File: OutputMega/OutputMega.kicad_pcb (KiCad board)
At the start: 2 copper layers, 78.7 x 92.1 mm, 134 parts, among them J1 Control, J10 Conn_02x13_Top_Bottom, J11 EStop Sig1 JST2H, J12 MegaProMiniR, J13 JTAG, J14 Dbg, J15 EStop Rly JST2H, J16 Sp Rly 1 JST2H, J17 Sp Rly 2 JST2H, J18 Step Disable JST2H, J19 EStop Sig0 JST2H, J2 EStop JST3H, J20 EStop Sig1 JST2H, J21 Conn_01x06_Male, J22 Conn_02x05_Odd_Even, J23 Sw 12v 1 JST2H, J24 Sw 12v 2 JST2H, J25 Pilot JST2H, J26 VFD Dir JST3H, J27 VFD Ctl JST3H, J3 EStop Rst JST2H, J4 TmrTest, J5 DbgPort, J6 RemPort, J7 12VIn, J8 PwrIn, J9 MegaProMiniL, K1 G6S-2, K2 G6S-2, K3 G6S-2, Q1 2N7002, Q10 2N7002, Q11 2N7002, Q12 2N7002, Q13 2N7002, Q2 2N7002, Q3 2N7002, Q4 2N7002, Q5 2N7002, Q6 2N7002, Q7 2N7002, Q8 2N7002, Q9 2N7002, U1 74HCT123, U10 MC34072AP, U2 74LS08, U3 LD1117S50TR_SOT223, U4 74LVC2G00, U5 74AUC2G34, U6 74AUC2G34, U7 74LVC2G157, U8 74LS08, U9 TLV9351

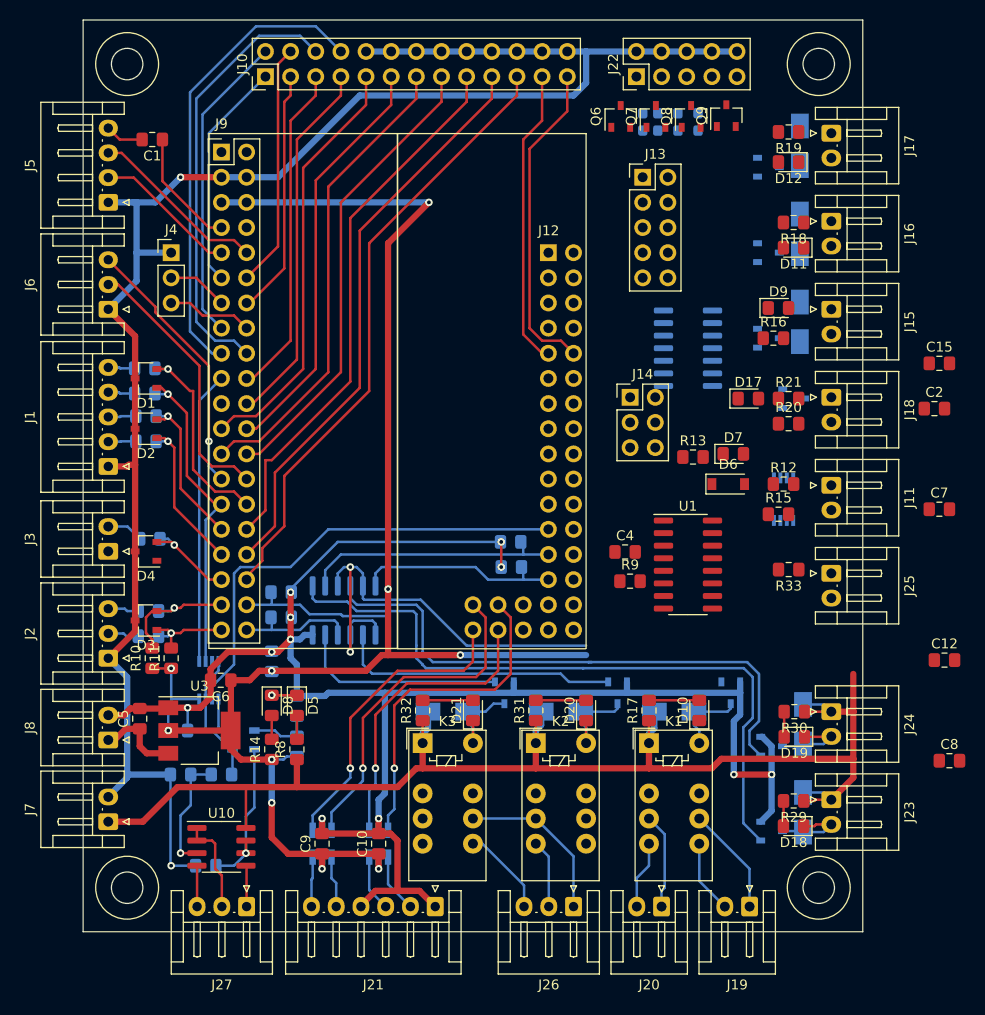
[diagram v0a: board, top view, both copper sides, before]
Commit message: Output Mega layout completed.
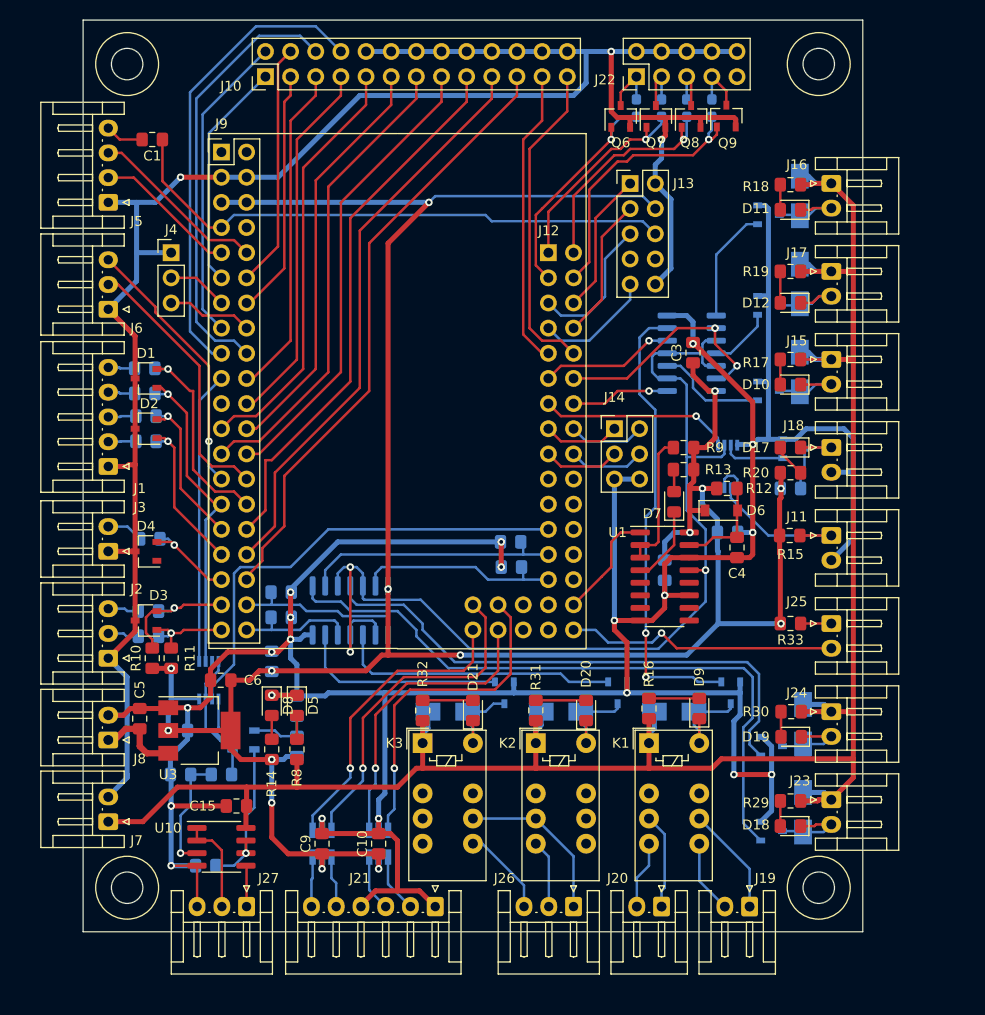
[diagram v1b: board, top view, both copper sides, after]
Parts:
- removed C8: .1uf, Capacitor_SMD:C_0805_2012Metric_Pad1.15x1.40mm_HandSolder
- C12, C2, C7, R21: moved to B.Cu
- C3: moved to F.Cu
- J1: footprint Connector_JST:JST_EH_S5B-EH_1x05_P2.50mm_Horizontal -> 0MiscParts:JST_EH_S5B-EH_1x05_P2.50mm_Horizontal
- J11, J15, J16, J17, J18, J19, J20, J23, J24, J25, J3, J7, J8: footprint Connector_JST:JST_EH_S2B-EH_1x02_P2.50mm_Horizontal -> 0MiscParts:JST_EH_S2B-EH_1x02_P2.50mm_Horizontal
- J2, J26, J27, J6: footprint Connector_JST:JST_EH_S3B-EH_1x03_P2.50mm_Horizontal -> 0MiscParts:JST_EH_S3B-EH_1x03_P2.50mm_Horizontal
- J5: footprint Connector_JST:JST_EH_S4B-EH_1x04_P2.50mm_Horizontal -> 0MiscParts:JST_EH_S4B-EH_1x04_P2.50mm_Horizontal
- moved C15 83.9 mm to (103.8, 142.2), turned to 180 degrees
- moved C12 67.9 mm to (107.3, 127.6), turned to 90 degrees
- moved C3 52.7 mm to (149.9, 96.5)
- moved D9 41.2 mm to (150.5, 132.4), turned to 90 degrees
- moved R16 39.5 mm to (145.4, 132.4), turned to 90 degrees
- moved R17 38.2 mm to (159.7, 97.1), turned to 180 degrees
- moved D10 34.2 mm to (159.7, 99.7), turned to 180 degrees
- moved C2 31.8 mm to (147.0, 118.4), turned to 270 degrees
- moved C7 21.5 mm to (153.4, 114.6)
- moved R9 14.5 mm to (148.9, 106.0), turned to 180 degrees
- moved D12 14.2 mm to (159.7, 91.4)
- moved R19 14.1 mm to (159.7, 88.3)
- moved D16 14.0 mm to (160.7, 89.5)
- moved J17 14.0 mm to (163.8, 88.3)
- moved Q4 14.0 mm to (157.5, 91.7)
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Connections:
- net /EGR renamed /ESSR
- net /ESR renamed /ESRR
- net /EStopRlyDrv renamed /EStopRlyExt
- D17 pad 1: /DsR -> /StepDisDrv
- D17 pad 2: +5V -> /DsR
- R20 pad 1: /DsR -> +5V
- R20 pad 2: /StepDisDrv -> /DsR
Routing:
- net GND: track 380.0 -> 566.1 mm, vias 14 -> 23
- net +5V: track 161.7 -> 266.9 mm, vias 10 -> 15
- net +12V: track 137.2 -> 218.7 mm
- net /WDOut: track 46.7 -> 105.9 mm, vias 2 -> 3
- net /EStopSigOut: track 0.00 -> 46.4 mm, vias 0 -> 2
- net /Reset: track 12.1 -> 57.2 mm
- net /Ctl4Out: track 0.00 -> 27.9 mm, vias 0 -> 1
- net /Pilot: track 0.00 -> 27.6 mm, vias 0 -> 1
- net /ProcSpindleRly: track 0.00 -> 23.7 mm, vias 0 -> 2
- net /Ctl1Out: track 0.00 -> 23.1 mm, vias 0 -> 1
- net /Ctl3Out: track 0.00 -> 22.9 mm, vias 0 -> 1
- net /Ctl2Out: track 0.00 -> 21.2 mm, vias 0 -> 1
- net /ProcStepDis: track 0.00 -> 19.3 mm, vias 0 -> 1
- net /ExtStepDis: track 0.00 -> 15.9 mm
- net /TDO: track 0.00 -> 14.4 mm
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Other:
- net class Power added: clearance 0.2032, trace_width 0.508, via_dia 0.762, via_drill 0.381

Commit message: Add labels to silk screen.
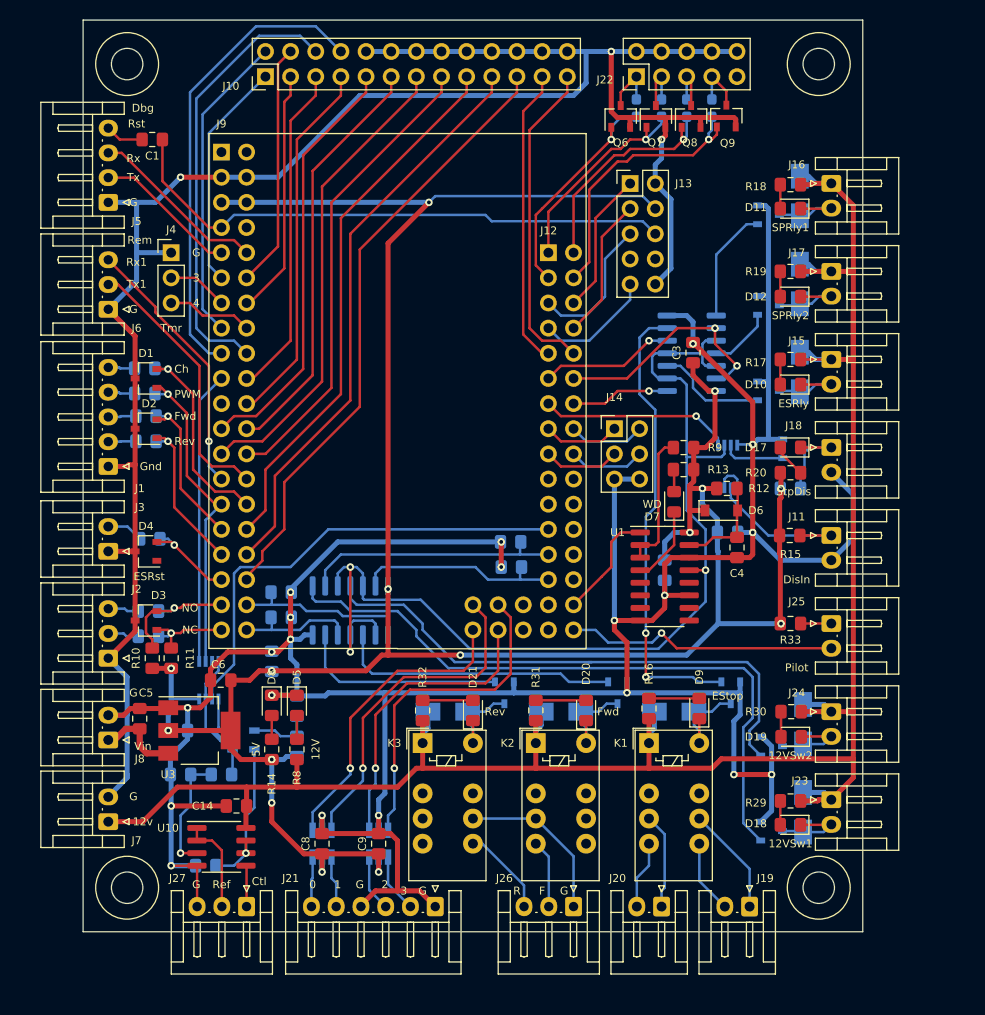
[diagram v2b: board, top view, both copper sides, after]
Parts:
- moved D12 0.62 mm to (159.7, 90.8)
- moved D18 0.13 mm to (159.7, 144.1)
- moved D11 0.11 mm to (159.7, 81.9)
- renumbered C11 to C10, C12 to C11, C13 to C12, C14 to C13, C15 to C14, C9 to C8, C10 to C9
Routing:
- net GND: track 566.1 -> 563.4 mm
- net /Sp2R: track 3.17 -> 2.55 mm
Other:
- board text added: "0"
- board text added: "1"
- board text added: "12V"
- board text added: "12VSw1"
- board text added: "12VSw2"
- board text added: "12v"
- board text added: "2"
- board text added: "3"
- board text added: "4"
- board text added: "5V"
- board text added: "Ch"
- board text added: "Ctl"
- board text added: "Dbg"
- board text added: "DisIn"
- board text added: "ESRly"
- board text added: "ESRst"
- board text added: "EStop"
- board text added: "F"
- board text added: "Fwd"
- board text added: "G"
- board text added: "Gnd"
- board text added: "NC"
- board text added: "NO"
- board text added: "PWM"
- board text added: "Pilot"
- board text added: "R"
- board text added: "Ref"
- board text added: "Rem"
- board text added: "Rev"
- board text added: "Rst"
- board text added: "Rx"
- board text added: "Rx1"
- board text added: "SPRly1"
- board text added: "SPRly2"
- board text added: "StpDis"
- board text added: "Tmr"
- board text added: "Tx"
- board text added: "Tx1"
- board text added: "Vin"
- board text added: "WD"

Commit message: Designed front panel.  More updates to output.
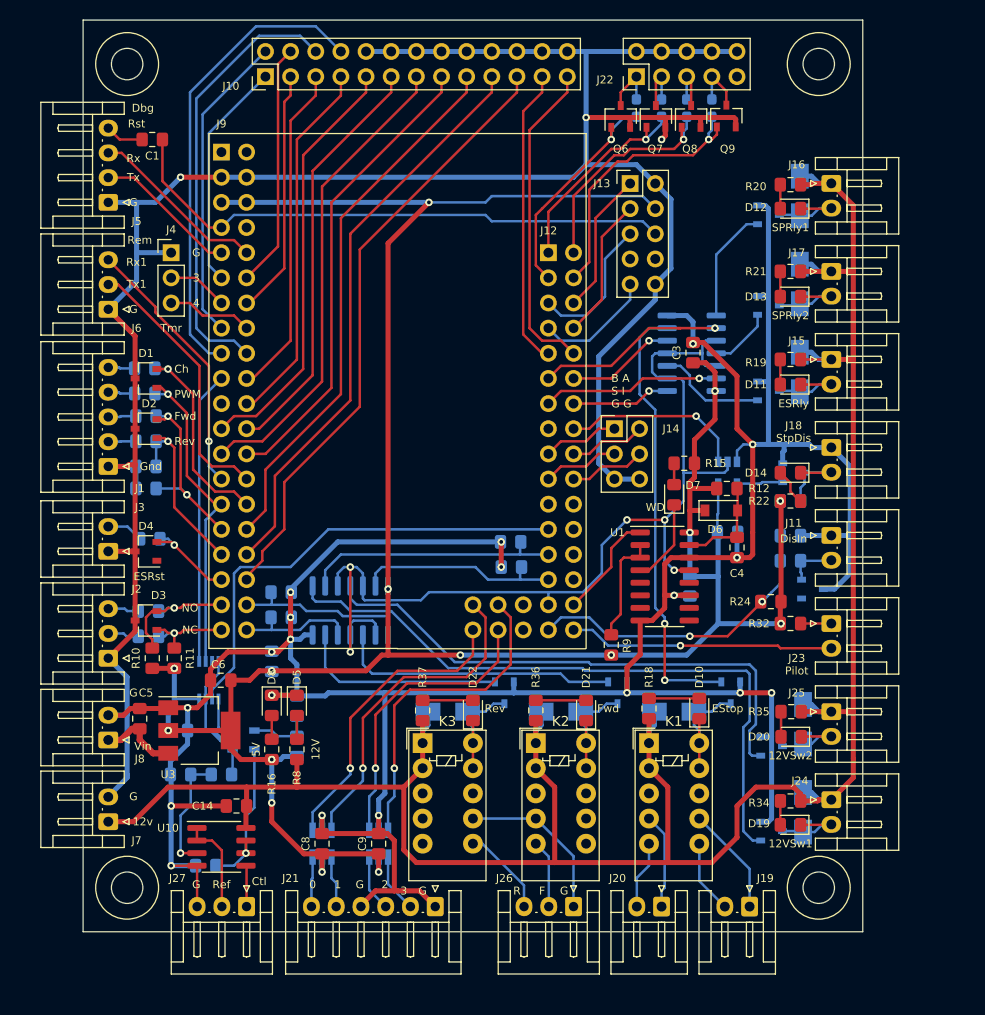
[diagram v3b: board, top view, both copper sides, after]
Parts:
- added D9: D_Zener_x2_ACom_KKA, 0MiscParts:SOT-23-Handsoldering, B.Cu at (161.9, 120.3)
- added R13: 10k, Resistor_SMD:R_0805_2012Metric_Pad1.15x1.40mm_HandSolder, B.Cu at (94.6, 110.2)
- added R14: 10k, Resistor_SMD:R_0805_2012Metric_Pad1.15x1.40mm_HandSolder, B.Cu at (94.6, 108.0)
- added R17: 200, Resistor_SMD:R_0805_2012Metric_Pad1.15x1.40mm_HandSolder, B.Cu at (159.7, 117.5)
- added R25: 10k, Resistor_SMD:R_0805_2012Metric_Pad1.15x1.40mm_HandSolder, B.Cu at (159.7, 114.9)
- J1: value Control -> Control JST5H
- J11: value EStop Sig1 JST2H -> Ext Step Disable JST2H
- J13: value JTAG -> JTAG 2x05
- J14: value Dbg -> Dbg 2x03
- J4: value TmrTest -> TmrTest 1x03
- J5: value DbgPort -> DbgPort JST4H
- J6: value RemPort -> RemPort JST3H
- J7: value 12VIn -> 12VIn JST2H
- J8: value PwrIn -> PwrIn JST2H
- K1, K2, K3: footprint Relay_THT:Relay_DPDT_Omron_G6S-2 -> 0MiscParts:Relay_DPDT_Omron_G6S-2
- R24: renamed from R15; value R -> 10k
- U4: value 74LVC2G00 -> 74LVC1G08; footprint Package_SO:TSSOP-8_3x3mm_P0.65mm -> Package_TO_SOT_SMD:SOT-23-5
- moved R9 21.2 mm to (141.6, 126.0), turned to 90 degrees
- moved R24 6.95 mm to (157.7, 121.6), turned to 180 degrees
- moved C2 3.00 mm to (149.5, 120.0)
- moved R22 2.86 mm to (159.7, 111.4)
- moved D14 2.55 mm to (159.7, 108.6)
- moved Q5 2.43 mm to (160.0, 108.6)
- moved R23 1.27 mm to (159.7, 111.4)
- moved D7 0.71 mm to (148.0, 110.8)
- moved R15 0.64 mm to (149.0, 107.6)
- moved U4 0.63 mm to (153.4, 108.6)
- moved R11 0.32 mm to (97.5, 127.3)
- renumbered D9 to D10, D10 to D11, D11 to D12, D12 to D13, D17 to D14, D13 to D15, D14 to D16, D15 to D17, D16 to D18, D18 to D19, D19 to D20, D20 to D21, D21 to D22, D22 to D23, D23 to D24, D24 to D25, D25 to D26, J25 to J23, J23 to J24, J24 to J25, R13 to R15, R14 to R16, R16 to R18, R17 to R19, R18 to R20, R19 to R21, R20 to R22, R21 to R23, R22 to R26, R23 to R27, R24 to R28, R25 to R29, R26 to R30, R27 to R31, R33 to R32, R28 to R33, R29 to R34, R30 to R35, R31 to R36, R32 to R37
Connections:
- J11 pad 1: /ExtStepDis -> GND
- J11 pad 2: GND -> /StepDisIn
- J12 pad 51: /ProcEStopSig -> /ProcSpdlRly1
- J12 pad 52: /ProcSpindleRly -> /ProcEStopSig
- J12 pad 53: /ProcStepDis -> /ProcSpdlRly2
- J12 pad 55: /B -> (no net)
- J12 pad 56: /A -> /ProcStepDis
- J12 pad 57: /Sync -> /B
- J12 pad 58: /Index -> /A
- J12 pad 59: (no net) -> /Sync
- J12 pad 60: (no net) -> /Index
- J12 pad 69: (no net) -> /WDOut
- J12 pad 71: (no net) -> /ExtStepDis
- J18 pad 1: /StepDisDrv -> GND
- J18 pad 2: GND -> /StepDisDrv
- U2 pad 13: /ProcSpindleRly -> /ProcSpdlRly2
- U2 pad 9: /ProcSpindleRly -> /ProcSpdlRly1
- U4 pad 3: /StepDis -> GND
- U4 pad 4: GND -> /StepDis
- U4 pad 5: /StepDisOut -> +5V
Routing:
- net +12V: track 218.7 -> 248.4 mm
- net /ProcSpindleRly: track 23.7 -> 0.00 mm, vias 2 -> 0
- net GND: track 563.4 -> 586.6 mm, vias 23 -> 22
- net /ProcSpdlRly1: track 0.00 -> 19.2 mm, vias 0 -> 1
- net /ProcSpdlRly2: track 0.00 -> 18.0 mm, vias 0 -> 1
- net /ExtStepDis: track 15.9 -> 31.8 mm, vias 0 -> 2
- net /StepDisIn: track 0.00 -> 5.07 mm
- net /WDOut: track 105.9 -> 101.5 mm, vias 3 -> 5
- net /SpFwd: track 16.1 -> 19.5 mm, vias 1 -> 2
- net /StepDisOut: track 3.31 -> 0.00 mm
- net +5V: track 267.3 -> 264.4 mm
- net /WDPU: track 13.9 -> 11.2 mm
- net /RevDrv: track 9.72 -> 12.3 mm
- net /FwdDrv: track 9.72 -> 12.3 mm
- net /EStopRly: track 9.91 -> 12.5 mm
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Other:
- board text added: "B A S I G G"

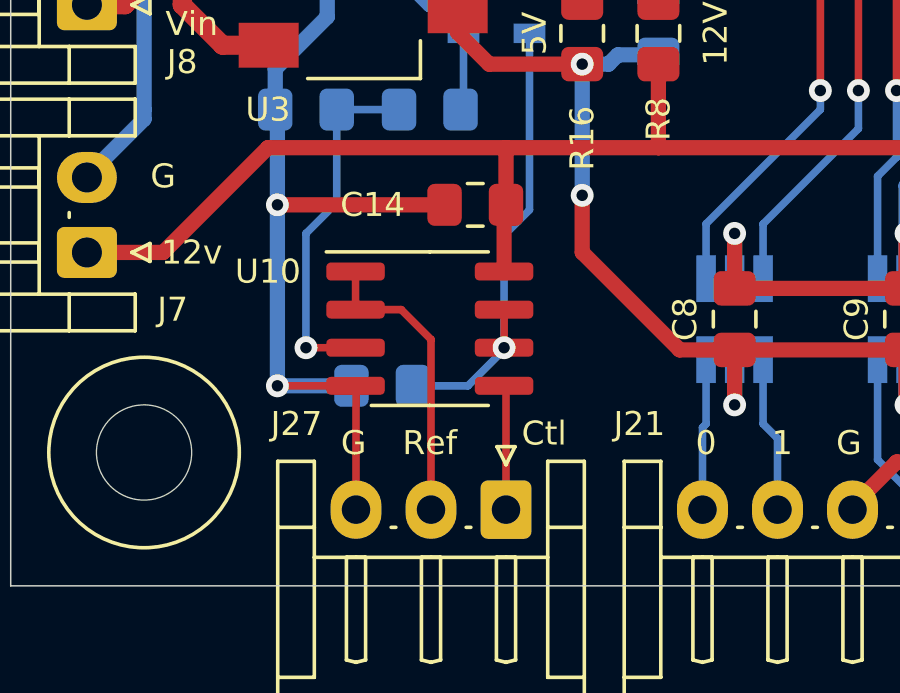
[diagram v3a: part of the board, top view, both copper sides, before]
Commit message: Add ferrite and capacitor to filter VFD control voltage.
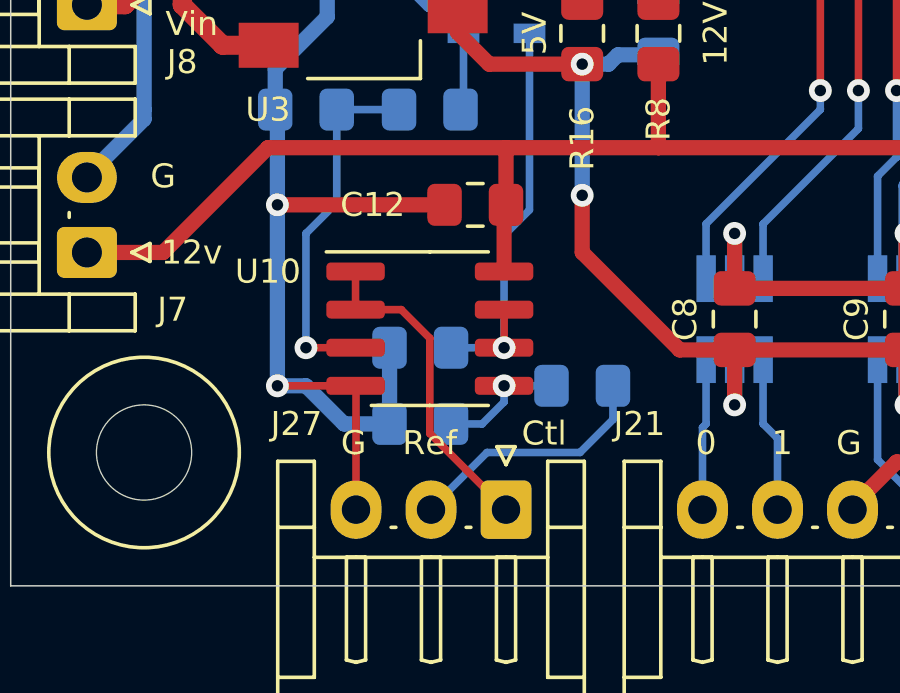
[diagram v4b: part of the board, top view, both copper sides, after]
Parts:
- added C15: .1uf, Capacitor_SMD:C_0805_2012Metric_Pad1.15x1.40mm_HandSolder, B.Cu at (101.9, 149.5)
- added FB1: Ferrite_Bead, Inductor_SMD:L_0805_2012Metric_Pad1.15x1.40mm_HandSolder, B.Cu at (107.3, 148.3)
- moved C13 1.80 mm to (101.9, 147.0)
- renumbered C14 to C12, C12 to C13, C13 to C14
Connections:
- J27 pad 2: /RefIn -> /MaxV
- U10 pad 1: /RefIn -> /CtlV
- U10 pad 2: /RefIn -> /CtlV
- U10 pad 5: /CtlV -> /MaxVFilt
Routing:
- net /RefIn: track 9.87 -> 0.00 mm
- net /MaxV: track 0.00 -> 8.46 mm
- net /CtlV: track 4.15 -> 10.9 mm
- net GND: track 586.6 -> 590.9 mm
- net /MaxVFilt: track 0.00 -> 4.28 mm, vias 0 -> 1
- net /PWMV+: track 15.7 -> 13.9 mm

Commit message: Boards sent to be built.
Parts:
- added JP5: SolderJumper_3_Open, 0MiscParts:Jumper_0603_3, B.Cu at (107.6, 148.3)
- added R38: R, Resistor_SMD:R_0805_2012Metric_Pad1.15x1.40mm_HandSolder, F.Cu at (106.7, 141.4)
- added U11: LM4040DBZ-10, 0MiscParts:SOT-23-Handsoldering, F.Cu at (109.5, 144.0)
- U4: value 74LVC1G08 -> 74LVC1G00
- moved FB1 5.02 mm to (102.6, 149.9), turned to 0 degrees
- moved C15 2.86 mm to (101.9, 146.7)
- moved C13 2.54 mm to (101.9, 144.5)
- moved U9 0.95 mm to (103.5, 135.6)
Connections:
- U10 pad 5: /MaxVFilt -> /PWMRef
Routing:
- net /PWMRef: track 6.55 -> 24.2 mm, vias 0 -> 1
- net /MaxV: track 8.46 -> 2.85 mm
- net /IntRef: track 0.00 -> 5.49 mm, vias 0 -> 1
- net /MaxVFilt: track 4.28 -> 7.56 mm, vias 1 -> 0
- net GND: track 590.9 -> 592.1 mm
- net /PWMSig: track 4.43 -> 3.38 mm
